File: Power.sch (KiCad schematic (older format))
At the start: 12 parts, among them J10 CONN_01X03, J11 test, J12 test, U10 LT1118-5V

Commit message: 전해콘덴서 foot print 변경
전해 콘덴서 변경
Bypass 콘데서 OPAMP에 추가 하여야 함
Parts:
- C43, C45: footprint Capacitors_SMD:C_1812_HandSoldering -> USER:C_1812_HandSoldering_Polar
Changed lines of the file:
@@
 F 0 "C45" H 6925 3850 50  0000 L CNN
 F 1 "10uF" H 6925 3650 50  0000 L CNN
-F 2 "Capacitors_SMD:C_1812_HandSoldering" H 6900 3750 50  0001 C CNN
+F 2 "USER:C_1812_HandSoldering_Polar" H 6900 3750 50  0001 C CNN
 F 3 "" H 6900 3750 50  0001 C CNN
 	1    6900 3750
@@
 F 0 "C43" H 5125 3850 50  0000 L CNN
 F 1 "10uF" H 5125 3650 50  0000 L CNN
-F 2 "Capacitors_SMD:C_1812_HandSoldering" H 5100 3750 50  0001 C CNN
+F 2 "USER:C_1812_HandSoldering_Polar" H 5100 3750 50  0001 C CNN
 F 3 "" H 5100 3750 50  0001 C CNN
 	1    5100 3750

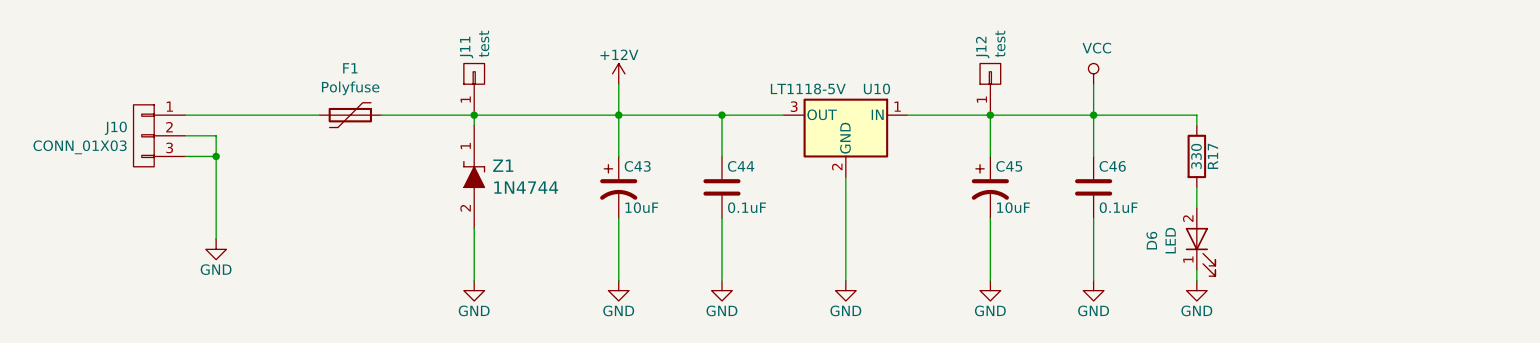
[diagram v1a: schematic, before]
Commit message: 2차 PCB 1차 수정
1. ADR455 Vcc V12 수정
2. DCDC 입력전압 변경
3. Bypass 콘덴서 C66, C67 추가
4. SOIC 방향 표시
5. TLV431 PADS 변경
6. AQV258 Pin3 --> Pin2
7. 전해콘덴서 방향추가
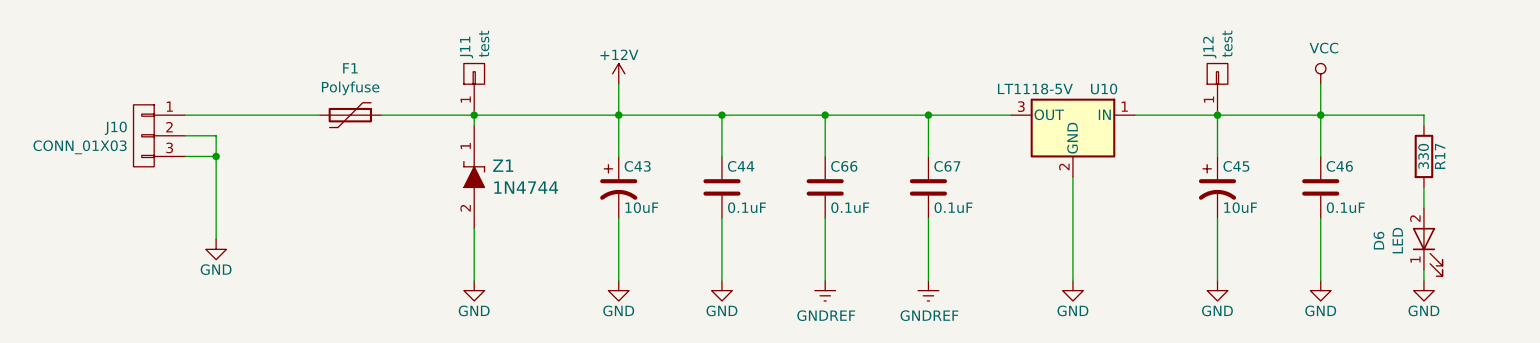
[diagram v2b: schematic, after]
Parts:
- added C66, C67: 0.1uF, Capacitors_SMD:C_0805_HandSoldering, symbol C
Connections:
- net +12V: now also C66.1, C67.1
- new net GNDREF: C66.2, C67.2
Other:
- moved on the sheet: C45, C46, D6, J12, R17, U10
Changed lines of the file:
@@
 L L7805 U10
 U 1 1 5ACF8FB6
-P 6200 3400
-F 0 "U10" H 6050 3525 50  0000 C CNN
-F 1 "LT1118-5V" H 6200 3525 50  0000 L CNN
-F 2 "TO_SOT_Packages_SMD:SOT-223" H 6225 3250 50  0001 L CIN
-F 3 "" H 6200 3350 50  0001 C CNN
-	1    6200 3400
+P 7300 3400
+F 0 "U10" H 7150 3525 50  0000 C CNN
+F 1 "LT1118-5V" H 7300 3525 50  0000 L CNN
+F 2 "TO_SOT_Packages_SMD:SOT-223" H 7325 3250 50  0001 L CIN
+F 3 "" H 7300 3350 50  0001 C CNN
+	1    7300 3400
 	-1   0    0    -1
 $EndComp
@@
 L CP1 C45
 U 1 1 5ACF8FBD
-P 6900 3750
-F 0 "C45" H 6925 3850 50  0000 L CNN
-F 1 "10uF" H 6925 3650 50  0000 L CNN
-F 2 "USER:C_1812_HandSoldering_Polar" H 6900 3750 50  0001 C CNN
-F 3 "" H 6900 3750 50  0001 C CNN
-	1    6900 3750
+P 8000 3750
+F 0 "C45" H 8025 3850 50  0000 L CNN
+F 1 "10uF" H 8025 3650 50  0000 L CNN
+F 2 "USER:C_1812_HandSoldering_Polar" H 8000 3750 50  0001 C CNN
+F 3 "" H 8000 3750 50  0001 C CNN
+	1    8000 3750
 	1    0    0    -1
 $EndComp
@@
 L GND #PWR080
 U 1 1 5ACF8FC4
-P 6900 4200
-F 0 "#PWR080" H 6900 3950 50  0001 C CNN
-F 1 "GND" H 6900 4050 50  0000 C CNN
-F 2 "" H 6900 4200 50  0001 C CNN
-F 3 "" H 6900 4200 50  0001 C CNN
-	1    6900 4200
+P 8000 4200
+F 0 "#PWR080" H 8000 3950 50  0001 C CNN
+F 1 "GND" H 8000 4050 50  0000 C CNN
+F 2 "" H 8000 4200 50  0001 C CNN
+F 3 "" H 8000 4200 50  0001 C CNN
+	1    8000 4200
 	1    0    0    -1
 $EndComp
@@
 L GND #PWR079
 U 1 1 5ACF8FCA
-P 6200 4200
-F 0 "#PWR079" H 6200 3950 50  0001 C CNN
-F 1 "GND" H 6200 4050 50  0000 C CNN
-F 2 "" H 6200 4200 50  0001 C CNN
-F 3 "" H 6200 4200 50  0001 C CNN
-	1    6200 4200
+P 7300 4200
+F 0 "#PWR079" H 7300 3950 50  0001 C CNN
+F 1 "GND" H 7300 4050 50  0000 C CNN
+F 2 "" H 7300 4200 50  0001 C CNN
+F 3 "" H 7300 4200 50  0001 C CNN
+	1    7300 4200
 	1    0    0    -1
 $EndComp
@@
 L VCC #PWR081
 U 1 1 5ACF8FE9
-P 7400 3250
-F 0 "#PWR081" H 7400 3100 50  0001 C CNN
-F 1 "VCC" H 7417 3423 50  0000 C CNN
-F 2 "" H 7400 3250 50  0001 C CNN
-F 3 "" H 7400 3250 50  0001 C CNN
-	1    7400 3250
+P 8500 3250
+F 0 "#PWR081" H 8500 3100 50  0001 C CNN
+F 1 "VCC" H 8517 3423 50  0000 C CNN
+F 2 "" H 8500 3250 50  0001 C CNN
+F 3 "" H 8500 3250 50  0001 C CNN
+	1    8500 3250
 	1    0    0    -1
 $EndComp
@@
 L GND #PWR082
 U 1 1 5ACF8FF6
-P 7400 4200
-F 0 "#PWR082" H 7400 3950 50  0001 C CNN
-F 1 "GND" H 7400 4050 50  0000 C CNN
-F 2 "" H 7400 4200 50  0001 C CNN
-F 3 "" H 7400 4200 50  0001 C CNN
-	1    7400 4200
+P 8500 4200
+F 0 "#PWR082" H 8500 3950 50  0001 C CNN
+F 1 "GND" H 8500 4050 50  0000 C CNN
+F 2 "" H 8500 4200 50  0001 C CNN
+F 3 "" H 8500 4200 50  0001 C CNN
+	1    8500 4200
 	1    0    0    -1
 $EndComp
@@
 L C C46
 U 1 1 5ACF8FFC
-P 7400 3750
-F 0 "C46" H 7425 3850 50  0000 L CNN
-F 1 "0.1uF" H 7425 3650 50  0000 L CNN
-F 2 "Capacitors_SMD:C_0805_HandSoldering" H 7438 3600 50  0001 C CNN
-F 3 "" H 7400 3750 50  0001 C CNN
-	1    7400 3750
-	1    0    0    -1
-$EndComp
-Wire Wire Line
-	6900 3400 6900 3600
-Wire Wire Line
-	6200 3700 6200 4200
+P 8500 3750
+F 0 "C46" H 8525 3850 50  0000 L CNN
+F 1 "0.1uF" H 8525 3650 50  0000 L CNN
+F 2 "Capacitors_SMD:C_0805_HandSoldering" H 8538 3600 50  0001 C CNN
+F 3 "" H 8500 3750 50  0001 C CNN
+	1    8500 3750
+	1    0    0    -1
+$EndComp
+Wire Wire Line
+	8000 3400 8000 3600
+Wire Wire Line
+	7300 3700 7300 4200
 Wire Wire Line
 	5100 3250 5100 3600
@@
 Wire Wire Line
 	5600 3900 5600 4200
-Connection ~ 6900 3400
-Wire Wire Line
-	6500 3400 7900 3400
+Connection ~ 8000 3400
+Wire Wire Line
+	7600 3400 9000 3400
 Connection ~ 5100 3400
-Connection ~ 7400 3400
-Wire Wire Line
-	6900 3900 6900 4200
+Connection ~ 8500 3400
+Wire Wire Line
+	8000 3900 8000 4200
 Wire Wire Line
 	5100 3900 5100 4200
 Wire Wire Line
-	7400 3900 7400 4200
-Wire Wire Line
-	7400 3250 7400 3600
+	8500 3900 8500 4200
+Wire Wire Line
+	8500 3250 8500 3600
 $Comp
 L 1N5231BTR Z1
@@
 	3000 3400 3650 3400
 Wire Wire Line
-	3950 3400 5900 3400
+	3950 3400 7000 3400
 $Comp
 L LED D6
 U 1 1 5ACFAB82
-P 7900 4000
-F 0 "D6" H 7891 4216 50  0000 C CNN
-F 1 "LED" H 7891 4125 50  0000 C CNN
-F 2 "LEDs:LED_D5.0mm" H 7900 4000 50  0001 C CNN
-F 3 "" H 7900 4000 50  0001 C CNN
-	1    7900 4000
+P 9000 4000
+F 0 "D6" H 8991 4216 50  0000 C CNN
+F 1 "LED" H 8991 4125 50  0000 C CNN
+F 2 "LEDs:LED_D5.0mm" H 9000 4000 50  0001 C CNN
+F 3 "" H 9000 4000 50  0001 C CNN
+	1    9000 4000
 	0    -1   -1   0
 $EndComp
@@
 L R R17
 U 1 1 5ACFAB89
-P 7900 3600
-F 0 "R17" V 7980 3600 50  0000 C CNN
-F 1 "330" V 7900 3600 50  0000 C CNN
-F 2 "Resistors_SMD:R_0805_HandSoldering" V 7830 3600 50  0001 C CNN
-F 3 "" H 7900 3600 50  0001 C CNN
-	1    7900 3600
-	1    0    0    -1
-$EndComp
-Wire Wire Line
-	7900 3400 7900 3450
-Wire Wire Line
-	7900 3750 7900 3850
+P 9000 3600
+F 0 "R17" V 9080 3600 50  0000 C CNN
+F 1 "330" V 9000 3600 50  0000 C CNN
+F 2 "Resistors_SMD:R_0805_HandSoldering" V 8930 3600 50  0001 C CNN
+F 3 "" H 9000 3600 50  0001 C CNN
+	1    9000 3600
+	1    0    0    -1
+$EndComp
+Wire Wire Line
+	9000 3400 9000 3450
+Wire Wire Line
+	9000 3750 9000 3850
 $Comp
 L GND #PWR083
 U 1 1 5ACFADFD
-P 7900 4200
-F 0 "#PWR083" H 7900 3950 50  0001 C CNN
-F 1 "GND" H 7900 4050 50  0000 C CNN
-F 2 "" H 7900 4200 50  0001 C CNN
-F 3 "" H 7900 4200 50  0001 C CNN
-	1    7900 4200
-	1    0    0    -1
-$EndComp
-Wire Wire Line
-	7900 4200 7900 4150
+P 9000 4200
+F 0 "#PWR083" H 9000 3950 50  0001 C CNN
+F 1 "GND" H 9000 4050 50  0000 C CNN
+F 2 "" H 9000 4200 50  0001 C CNN
+F 3 "" H 9000 4200 50  0001 C CNN
+	1    9000 4200
+	1    0    0    -1
+$EndComp
+Wire Wire Line
+	9000 4200 9000 4150
 $Comp
 L CONN_01X01 J12
 U 1 1 5B09207B
-P 6900 3200
+P 8000 3200
 AR Path="/5B09207B" Ref="J12"  Part="1"
 AR Path="/5A038739/5B09207B" Ref="J12"  Part="1"
-F 0 "J12" H 6979 3242 50  0000 L CNN
-F 1 "test" H 6979 3151 50  0000 L CNN
-F 2 "Pin_Headers:Pin_Header_Straight_1x01_Pitch2.00mm" H 6900 3200 50  0001 C CNN
-F 3 "~" H 6900 3200 50  0001 C CNN
-	1    6900 3200
+F 0 "J12" H 8079 3242 50  0000 L CNN
+F 1 "test" H 8079 3151 50  0000 L CNN
+F 2 "Pin_Headers:Pin_Header_Straight_1x01_Pitch2.00mm" H 8000 3200 50  0001 C CNN
+F 3 "~" H 8000 3200 50  0001 C CNN
+	1    8000 3200
 	0    -1   -1   0
 $EndComp
@@
 	0    -1   -1   0
 $EndComp
+$Comp
+L C C66
+U 1 1 5B1E9998
+P 6100 3750
+F 0 "C66" H 6125 3850 50  0000 L CNN
+F 1 "0.1uF" H 6125 3650 50  0000 L CNN
+F 2 "Capacitors_SMD:C_0805_HandSoldering" H 6138 3600 50  0001 C CNN
+F 3 "" H 6100 3750 50  0001 C CNN
+	1    6100 3750
+	1    0    0    -1
+$EndComp
+Wire Wire Line
+	6100 3400 6100 3600
+Wire Wire Line
+	6100 3900 6100 4200
+$Comp
+L C C67
+U 1 1 5B1E99D0
+P 6600 3750
+F 0 "C67" H 6625 3850 50  0000 L CNN
+F 1 "0.1uF" H 6625 3650 50  0000 L CNN
+F 2 "Capacitors_SMD:C_0805_HandSoldering" H 6638 3600 50  0001 C CNN
+F 3 "" H 6600 3750 50  0001 C CNN
+	1    6600 3750
+	1    0    0    -1
+$EndComp
+Wire Wire Line
+	6600 3400 6600 3600
+Wire Wire Line
+	6600 3900 6600 4200
+Connection ~ 6600 3400
+Connection ~ 6100 3400
+$Comp
+L GNDREF #PWR0159
+U 1 1 5B1EDD46
+P 6600 4200
+F 0 "#PWR0159" H 6600 3950 50  0001 C CNN
+F 1 "GNDREF" H 6605 4027 50  0000 C CNN
+F 2 "" H 6600 4200 50  0001 C CNN
+F 3 "" H 6600 4200 50  0001 C CNN
+	1    6600 4200
+	1    0    0    -1
+$EndComp
+$Comp
+L GNDREF #PWR0160
+U 1 1 5B1EDD4C
+P 6100 4200
+F 0 "#PWR0160" H 6100 3950 50  0001 C CNN
+F 1 "GNDREF" H 6105 4027 50  0000 C CNN
+F 2 "" H 6100 4200 50  0001 C CNN
+F 3 "" H 6100 4200 50  0001 C CNN
+	1    6100 4200
+	1    0    0    -1
+$EndComp
 $EndSCHEMATC

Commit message: 0805_넓히기
기타 수정
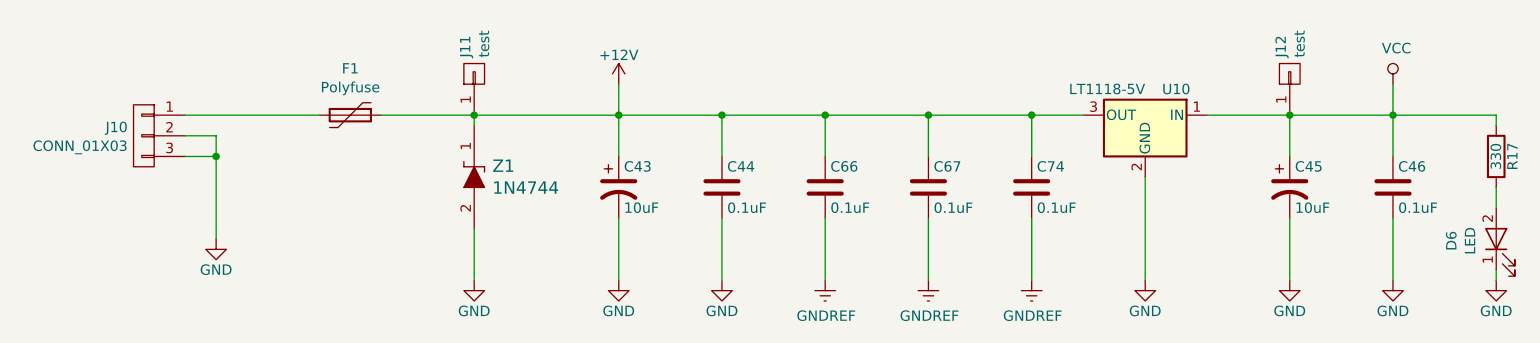
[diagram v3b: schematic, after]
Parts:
- added C74: 0.1uF, Capacitors_SMD:C_0805_HandSoldering, symbol C
- U10: footprint TO_SOT_Packages_SMD:SOT-223 -> USER:SOT-223_LT1118
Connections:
- net +12V: now also C74.1
- net GNDREF: now also C74.2
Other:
- moved on the sheet: C45, C46, D6, J12, R17, U10
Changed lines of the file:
@@
 L L7805 U10
 U 1 1 5ACF8FB6
-P 7300 3400
-F 0 "U10" H 7150 3525 50  0000 C CNN
-F 1 "LT1118-5V" H 7300 3525 50  0000 L CNN
-F 2 "TO_SOT_Packages_SMD:SOT-223" H 7325 3250 50  0001 L CIN
-F 3 "" H 7300 3350 50  0001 C CNN
-	1    7300 3400
+P 7650 3400
+F 0 "U10" H 7500 3525 50  0000 C CNN
+F 1 "LT1118-5V" H 7650 3525 50  0000 L CNN
+F 2 "USER:SOT-223_LT1118" H 7675 3250 50  0001 L CIN
+F 3 "" H 7650 3350 50  0001 C CNN
+	1    7650 3400
 	-1   0    0    -1
 $EndComp
@@
 L CP1 C45
 U 1 1 5ACF8FBD
-P 8000 3750
-F 0 "C45" H 8025 3850 50  0000 L CNN
-F 1 "10uF" H 8025 3650 50  0000 L CNN
-F 2 "USER:C_1812_HandSoldering_Polar" H 8000 3750 50  0001 C CNN
-F 3 "" H 8000 3750 50  0001 C CNN
-	1    8000 3750
+P 8350 3750
+F 0 "C45" H 8375 3850 50  0000 L CNN
+F 1 "10uF" H 8375 3650 50  0000 L CNN
+F 2 "USER:C_1812_HandSoldering_Polar" H 8350 3750 50  0001 C CNN
+F 3 "" H 8350 3750 50  0001 C CNN
+	1    8350 3750
 	1    0    0    -1
 $EndComp
@@
 L GND #PWR080
 U 1 1 5ACF8FC4
-P 8000 4200
-F 0 "#PWR080" H 8000 3950 50  0001 C CNN
-F 1 "GND" H 8000 4050 50  0000 C CNN
-F 2 "" H 8000 4200 50  0001 C CNN
-F 3 "" H 8000 4200 50  0001 C CNN
-	1    8000 4200
+P 8350 4200
+F 0 "#PWR080" H 8350 3950 50  0001 C CNN
+F 1 "GND" H 8350 4050 50  0000 C CNN
+F 2 "" H 8350 4200 50  0001 C CNN
+F 3 "" H 8350 4200 50  0001 C CNN
+	1    8350 4200
 	1    0    0    -1
 $EndComp
@@
 L GND #PWR079
 U 1 1 5ACF8FCA
-P 7300 4200
-F 0 "#PWR079" H 7300 3950 50  0001 C CNN
-F 1 "GND" H 7300 4050 50  0000 C CNN
-F 2 "" H 7300 4200 50  0001 C CNN
-F 3 "" H 7300 4200 50  0001 C CNN
-	1    7300 4200
+P 7650 4200
+F 0 "#PWR079" H 7650 3950 50  0001 C CNN
+F 1 "GND" H 7650 4050 50  0000 C CNN
+F 2 "" H 7650 4200 50  0001 C CNN
+F 3 "" H 7650 4200 50  0001 C CNN
+	1    7650 4200
 	1    0    0    -1
 $EndComp
@@
 L VCC #PWR081
 U 1 1 5ACF8FE9
-P 8500 3250
-F 0 "#PWR081" H 8500 3100 50  0001 C CNN
-F 1 "VCC" H 8517 3423 50  0000 C CNN
-F 2 "" H 8500 3250 50  0001 C CNN
-F 3 "" H 8500 3250 50  0001 C CNN
-	1    8500 3250
+P 8850 3250
+F 0 "#PWR081" H 8850 3100 50  0001 C CNN
+F 1 "VCC" H 8867 3423 50  0000 C CNN
+F 2 "" H 8850 3250 50  0001 C CNN
+F 3 "" H 8850 3250 50  0001 C CNN
+	1    8850 3250
 	1    0    0    -1
 $EndComp
@@
 L GND #PWR082
 U 1 1 5ACF8FF6
-P 8500 4200
-F 0 "#PWR082" H 8500 3950 50  0001 C CNN
-F 1 "GND" H 8500 4050 50  0000 C CNN
-F 2 "" H 8500 4200 50  0001 C CNN
-F 3 "" H 8500 4200 50  0001 C CNN
-	1    8500 4200
+P 8850 4200
+F 0 "#PWR082" H 8850 3950 50  0001 C CNN
+F 1 "GND" H 8850 4050 50  0000 C CNN
+F 2 "" H 8850 4200 50  0001 C CNN
+F 3 "" H 8850 4200 50  0001 C CNN
+	1    8850 4200
 	1    0    0    -1
 $EndComp
@@
 L C C46
 U 1 1 5ACF8FFC
-P 8500 3750
-F 0 "C46" H 8525 3850 50  0000 L CNN
-F 1 "0.1uF" H 8525 3650 50  0000 L CNN
-F 2 "Capacitors_SMD:C_0805_HandSoldering" H 8538 3600 50  0001 C CNN
-F 3 "" H 8500 3750 50  0001 C CNN
-	1    8500 3750
-	1    0    0    -1
-$EndComp
-Wire Wire Line
-	8000 3400 8000 3600
-Wire Wire Line
-	7300 3700 7300 4200
+P 8850 3750
+F 0 "C46" H 8875 3850 50  0000 L CNN
+F 1 "0.1uF" H 8875 3650 50  0000 L CNN
+F 2 "Capacitors_SMD:C_0805_HandSoldering" H 8888 3600 50  0001 C CNN
+F 3 "" H 8850 3750 50  0001 C CNN
+	1    8850 3750
+	1    0    0    -1
+$EndComp
+Wire Wire Line
+	8350 3400 8350 3600
+Wire Wire Line
+	7650 3700 7650 4200
 Wire Wire Line
 	5100 3250 5100 3600
@@
 Wire Wire Line
 	5600 3900 5600 4200
-Connection ~ 8000 3400
-Wire Wire Line
-	7600 3400 9000 3400
+Connection ~ 8350 3400
+Wire Wire Line
+	7950 3400 9350 3400
 Connection ~ 5100 3400
-Connection ~ 8500 3400
-Wire Wire Line
-	8000 3900 8000 4200
+Connection ~ 8850 3400
+Wire Wire Line
+	8350 3900 8350 4200
 Wire Wire Line
 	5100 3900 5100 4200
 Wire Wire Line
-	8500 3900 8500 4200
-Wire Wire Line
-	8500 3250 8500 3600
+	8850 3900 8850 4200
+Wire Wire Line
+	8850 3250 8850 3600
 $Comp
 L 1N5231BTR Z1
@@
 	3000 3400 3650 3400
 Wire Wire Line
-	3950 3400 7000 3400
+	3950 3400 7350 3400
 $Comp
 L LED D6
 U 1 1 5ACFAB82
-P 9000 4000
-F 0 "D6" H 8991 4216 50  0000 C CNN
-F 1 "LED" H 8991 4125 50  0000 C CNN
-F 2 "LEDs:LED_D5.0mm" H 9000 4000 50  0001 C CNN
-F 3 "" H 9000 4000 50  0001 C CNN
-	1    9000 4000
+P 9350 4000
+F 0 "D6" H 9341 4216 50  0000 C CNN
+F 1 "LED" H 9341 4125 50  0000 C CNN
+F 2 "LEDs:LED_D5.0mm" H 9350 4000 50  0001 C CNN
+F 3 "" H 9350 4000 50  0001 C CNN
+	1    9350 4000
 	0    -1   -1   0
 $EndComp
@@
 L R R17
 U 1 1 5ACFAB89
-P 9000 3600
-F 0 "R17" V 9080 3600 50  0000 C CNN
-F 1 "330" V 9000 3600 50  0000 C CNN
-F 2 "Resistors_SMD:R_0805_HandSoldering" V 8930 3600 50  0001 C CNN
-F 3 "" H 9000 3600 50  0001 C CNN
-	1    9000 3600
-	1    0    0    -1
-$EndComp
-Wire Wire Line
-	9000 3400 9000 3450
-Wire Wire Line
-	9000 3750 9000 3850
+P 9350 3600
+F 0 "R17" V 9430 3600 50  0000 C CNN
+F 1 "330" V 9350 3600 50  0000 C CNN
+F 2 "Resistors_SMD:R_0805_HandSoldering" V 9280 3600 50  0001 C CNN
+F 3 "" H 9350 3600 50  0001 C CNN
+	1    9350 3600
+	1    0    0    -1
+$EndComp
+Wire Wire Line
+	9350 3400 9350 3450
+Wire Wire Line
+	9350 3750 9350 3850
 $Comp
 L GND #PWR083
 U 1 1 5ACFADFD
-P 9000 4200
-F 0 "#PWR083" H 9000 3950 50  0001 C CNN
-F 1 "GND" H 9000 4050 50  0000 C CNN
-F 2 "" H 9000 4200 50  0001 C CNN
-F 3 "" H 9000 4200 50  0001 C CNN
-	1    9000 4200
-	1    0    0    -1
-$EndComp
-Wire Wire Line
-	9000 4200 9000 4150
+P 9350 4200
+F 0 "#PWR083" H 9350 3950 50  0001 C CNN
+F 1 "GND" H 9350 4050 50  0000 C CNN
+F 2 "" H 9350 4200 50  0001 C CNN
+F 3 "" H 9350 4200 50  0001 C CNN
+	1    9350 4200
+	1    0    0    -1
+$EndComp
+Wire Wire Line
+	9350 4200 9350 4150
 $Comp
 L CONN_01X01 J12
 U 1 1 5B09207B
-P 8000 3200
+P 8350 3200
 AR Path="/5B09207B" Ref="J12"  Part="1"
 AR Path="/5A038739/5B09207B" Ref="J12"  Part="1"
-F 0 "J12" H 8079 3242 50  0000 L CNN
-F 1 "test" H 8079 3151 50  0000 L CNN
-F 2 "Pin_Headers:Pin_Header_Straight_1x01_Pitch2.00mm" H 8000 3200 50  0001 C CNN
-F 3 "~" H 8000 3200 50  0001 C CNN
-	1    8000 3200
+F 0 "J12" H 8429 3242 50  0000 L CNN
+F 1 "test" H 8429 3151 50  0000 L CNN
+F 2 "Pin_Headers:Pin_Header_Straight_1x01_Pitch2.00mm" H 8350 3200 50  0001 C CNN
+F 3 "~" H 8350 3200 50  0001 C CNN
+	1    8350 3200
 	0    -1   -1   0
 $EndComp
@@
 	1    0    0    -1
 $EndComp
+$Comp
+L C C74
+U 1 1 5B2640B5
+P 7100 3750
+F 0 "C74" H 7125 3850 50  0000 L CNN
+F 1 "0.1uF" H 7125 3650 50  0000 L CNN
+F 2 "Capacitors_SMD:C_0805_HandSoldering" H 7138 3600 50  0001 C CNN
+F 3 "" H 7100 3750 50  0001 C CNN
+	1    7100 3750
+	1    0    0    -1
+$EndComp
+Wire Wire Line
+	7100 3400 7100 3600
+Wire Wire Line
+	7100 3900 7100 4200
+$Comp
+L GNDREF #PWR0166
+U 1 1 5B2640BE
+P 7100 4200
+F 0 "#PWR0166" H 7100 3950 50  0001 C CNN
+F 1 "GNDREF" H 7105 4027 50  0000 C CNN
+F 2 "" H 7100 4200 50  0001 C CNN
+F 3 "" H 7100 4200 50  0001 C CNN
+	1    7100 4200
+	1    0    0    -1
+$EndComp
+Connection ~ 7100 3400
 $EndSCHEMATC
